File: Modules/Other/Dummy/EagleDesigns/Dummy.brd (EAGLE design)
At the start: 100 x 80 mm, 1 part

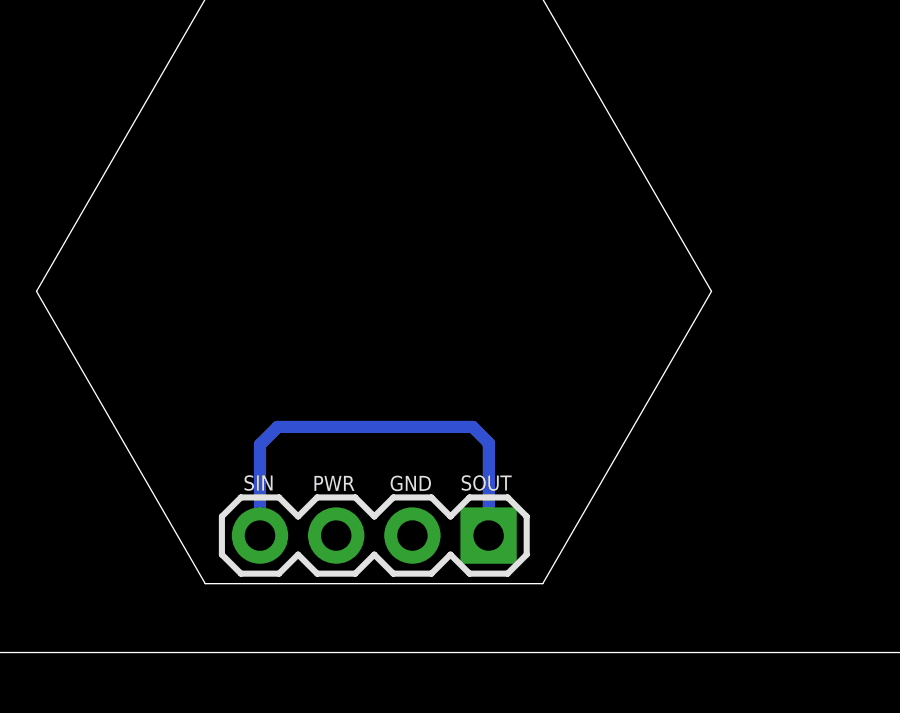
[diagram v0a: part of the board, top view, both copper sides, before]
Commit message: Added one single Board Layout for WireSEND, WireRECV, and Dummy module
it now has a small jumper that could be soldered in order to connect
SIN to SOUT.
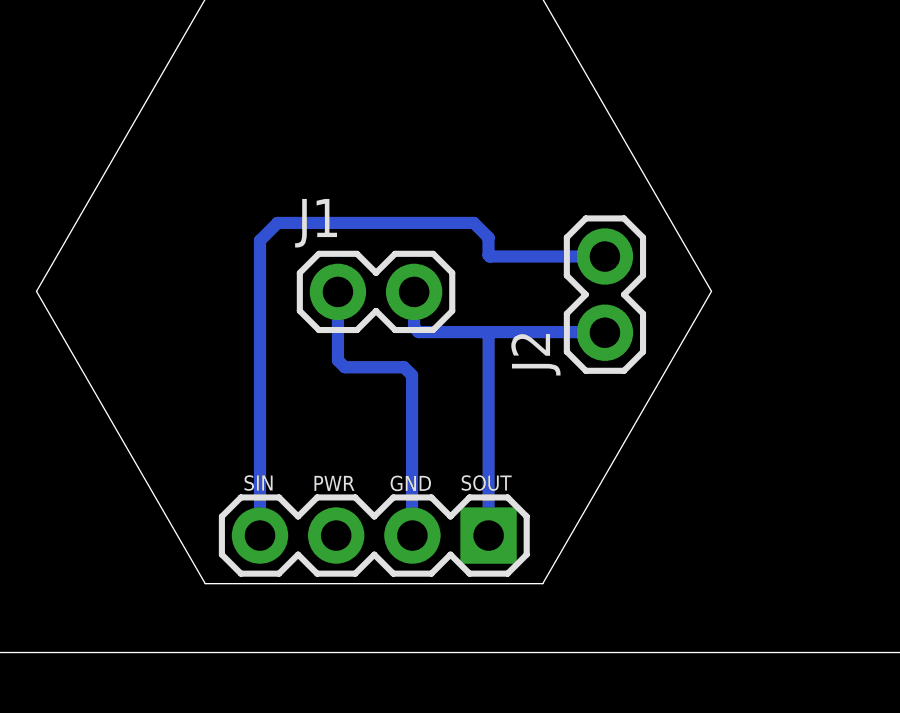
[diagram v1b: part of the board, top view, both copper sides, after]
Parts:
- added J1, J2: (no value), SparkFun-Connectors:1X02
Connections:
- removed net SIN-SOUT: JP1.1, JP1.4
- new net SIN: J2.2, JP1.4
- new net SOUT: J1.2, J2.1, JP1.1
- net GND: now also J1.1
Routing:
- net SIN: track 0.00 -> 22.4 mm
- net SOUT: track 0.00 -> 14.4 mm
- net SIN-SOUT: track 14.2 -> 0.00 mm
- net GND: track 0.06 -> 10.4 mm
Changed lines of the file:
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@@
 <attribute name="VALUE" x="18.4023" y="7.0739" size="1.27" layer="27" rot="R180"/>
 </element>
+<element name="J2" library="SparkFun-Connectors" package="1X02" value="" x="21.01" y="10.66" rot="R90"/>
+<element name="J1" library="SparkFun-Connectors" package="1X02" value="" x="12.11" y="12.02"/>
 </elements>
 <signals>
@@
 <contactref element="JP1" pad="2"/>
 <wire x1="14.55" y1="3.9412" x2="14.5923" y2="3.8989" width="0.3048" layer="16"/>
+<contactref element="J1" pad="1"/>
+<wire x1="12.11" y1="12.02" x2="12.11" y2="9.74" width="0.4064" layer="16"/>
+<wire x1="12.11" y1="9.74" x2="12.34" y2="9.51" width="0.4064" layer="16"/>
+<wire x1="12.34" y1="9.51" x2="14.31" y2="9.51" width="0.4064" layer="16"/>
+<wire x1="14.31" y1="9.51" x2="14.58" y2="9.24" width="0.4064" layer="16"/>
+<wire x1="14.58" y1="9.24" x2="14.58" y2="3.9112" width="0.4064" layer="16"/>
+<wire x1="14.58" y1="3.9112" x2="14.5923" y2="3.8989" width="0.4064" layer="16"/>
 </signal>
-<signal name="SIN-SOUT">
+<signal name="SIN">
 <contactref element="JP1" pad="4"/>
+<contactref element="J2" pad="2"/>
+<wire x1="9.5123" y1="3.8989" x2="9.5123" y2="13.7323" width="0.4064" layer="16"/>
+<wire x1="9.5123" y1="13.7323" x2="10.1" y2="14.32" width="0.4064" layer="16"/>
+<wire x1="10.1" y1="14.32" x2="16.64" y2="14.32" width="0.4064" layer="16"/>
+<wire x1="16.64" y1="14.32" x2="17.13" y2="13.83" width="0.4064" layer="16"/>
+<wire x1="17.13" y1="13.83" x2="17.13" y2="13.24" width="0.4064" layer="16"/>
+<wire x1="17.13" y1="13.24" x2="17.17" y2="13.2" width="0.4064" layer="16"/>
+<wire x1="17.17" y1="13.2" x2="21.01" y2="13.2" width="0.4064" layer="16"/>
+</signal>
+<signal name="SOUT">
 <contactref element="JP1" pad="1"/>
-<wire x1="9.5123" y1="3.8989" x2="9.5123" y2="6.9323" width="0.4064" layer="16"/>
-<wire x1="9.5123" y1="6.9323" x2="10.1" y2="7.52" width="0.4064" layer="16"/>
-<wire x1="10.1" y1="7.52" x2="16.6" y2="7.52" width="0.4064" layer="16"/>
-<wire x1="16.6" y1="7.52" x2="17.14" y2="6.98" width="0.4064" layer="16"/>
-<wire x1="17.14" y1="6.98" x2="17.14" y2="3.9066" width="0.4064" layer="16"/>
-<wire x1="17.14" y1="3.9066" x2="17.1323" y2="3.8989" width="0.4064" layer="16"/>
+<contactref element="J2" pad="1"/>
+<contactref element="J1" pad="2"/>
+<wire x1="14.65" y1="12.02" x2="14.65" y2="10.83" width="0.4064" layer="16"/>
+<wire x1="14.65" y1="10.83" x2="14.8" y2="10.68" width="0.4064" layer="16"/>
+<wire x1="14.8" y1="10.68" x2="17.09" y2="10.68" width="0.4064" layer="16"/>
+<wire x1="17.09" y1="10.68" x2="20.99" y2="10.68" width="0.4064" layer="16"/>
+<wire x1="20.99" y1="10.68" x2="21.01" y2="10.66" width="0.4064" layer="16"/>
+<wire x1="17.1323" y1="3.8989" x2="17.1323" y2="10.6377" width="0.4064" layer="16"/>
+<wire x1="17.1323" y1="10.6377" x2="17.09" y2="10.68" width="0.4064" layer="16"/>
 </signal>
 </signals>
